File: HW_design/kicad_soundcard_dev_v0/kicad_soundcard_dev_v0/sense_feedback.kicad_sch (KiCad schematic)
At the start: 18 parts, among them U4 LSM6DSL, U5 ICP20100

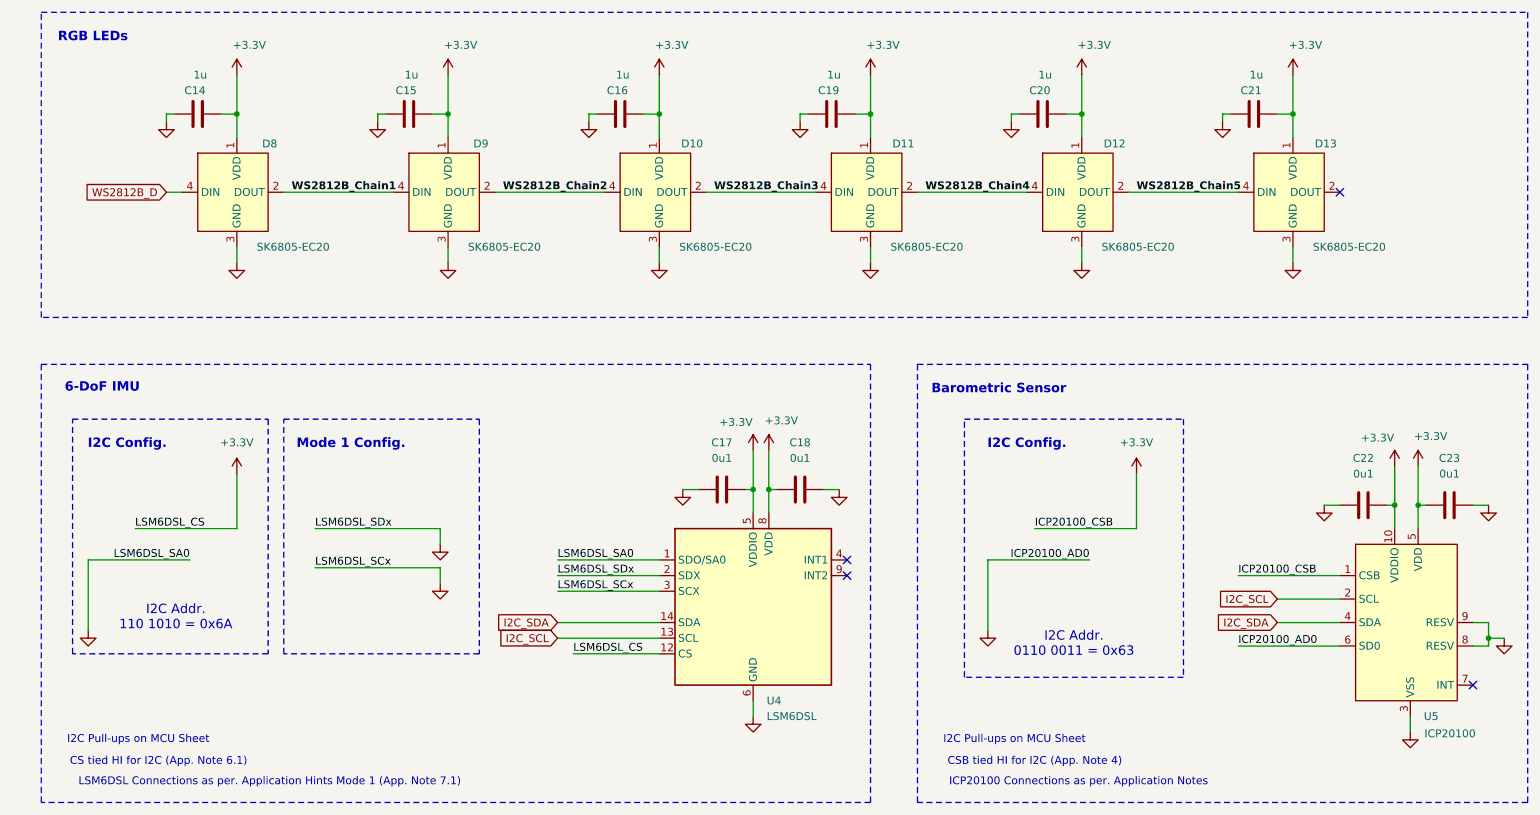
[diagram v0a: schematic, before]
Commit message: Schematic Rev2 + PCB Initial Release
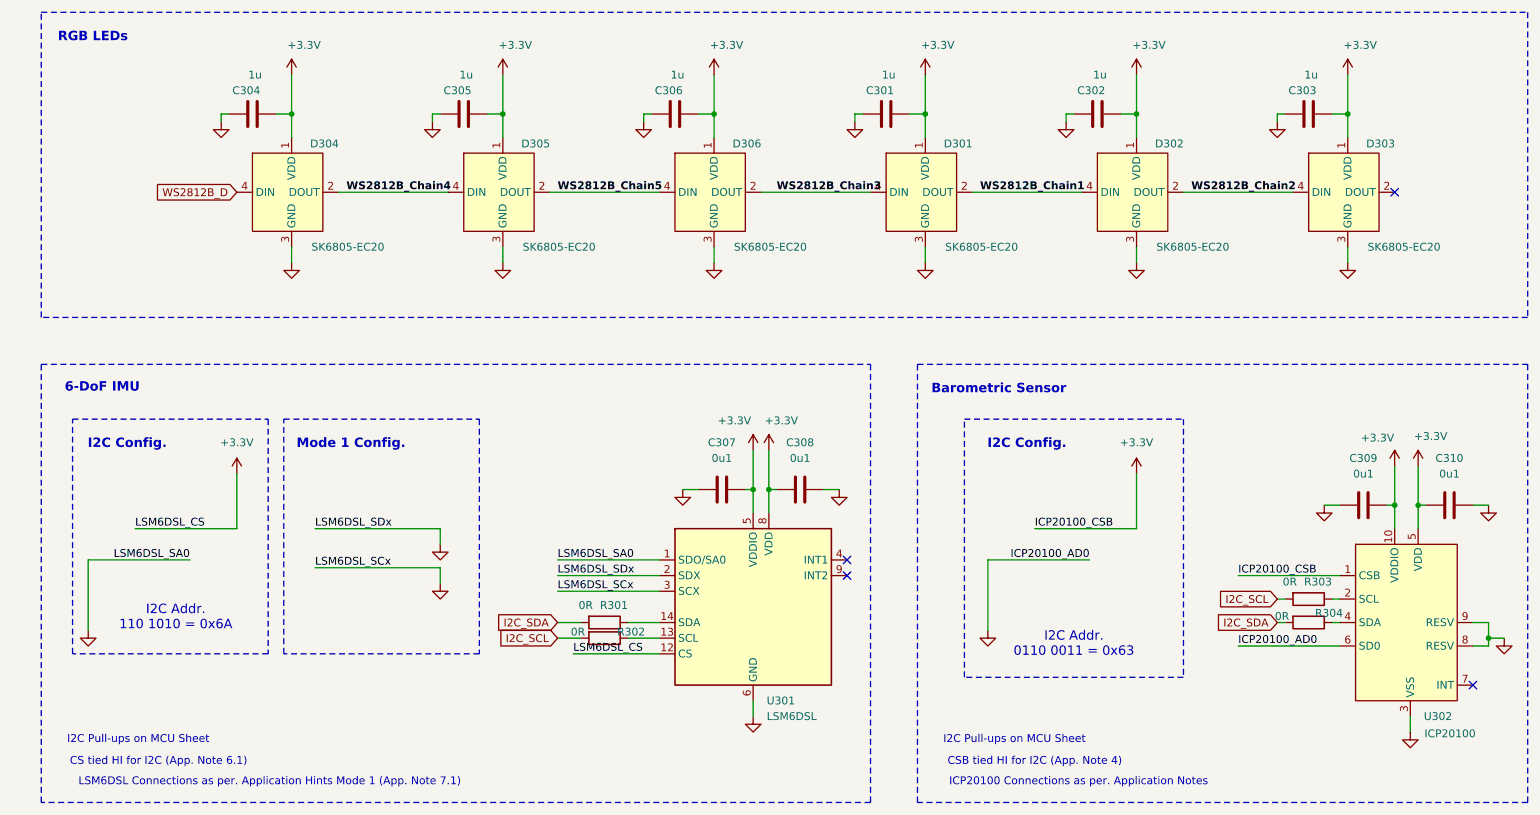
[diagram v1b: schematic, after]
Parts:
- added R301, R302, R303, R304: 0R, Resistor_SMD:R_0603_1608Metric, symbol Device:R
- renumbered C14 to C301, C15 to C302, C16 to C303, C19 to C304, C20 to C305, C21 to C306, C17 to C307, C18 to C308, C22 to C309, C23 to C310, D8 to D301, D9 to D302, D10 to D303, D11 to D304, D12 to D305, D13 to D306, U4 to U301, U5 to U302
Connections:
- net I2C_SCL: now also R302.2, R303.2; no longer U301.13 (SCL), U302.2 (SCL)
- net I2C_SDA: now also R301.2, R304.2; no longer U301.14 (SDA), U302.4 (SDA)
- net WS2812B_Chain3: now also D301.4 (DIN), D306.2 (DOUT); no longer D303.2 (DOUT), D304.4 (DIN)
- net WS2812B_D: now also D304.4 (DIN); no longer D301.4 (DIN)
- new net: R303.1, U302.2 (SCL)
- new net: R302.1, U301.13 (SCL)
- new net: R301.1, U301.14 (SDA)
- new net: R304.1, U302.4 (SDA)
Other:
- moved on the sheet: C301, C302, C303, C304, C305, C306, D301, D302, D303, D304, D305, D306

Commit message: Production JLCPCB V0
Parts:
- C301, C302, C303, C304, C305, C306: JLCPCB Link (none) -> https://jlcpcb.com/partdetail/15107-CL05A105KP5NNNC/C14445; Manufacturer (none) -> Samsung Electro-Mechanics; Manufacturer P/N (none) -> CL05A105KP5NNNC
- C307, C308, C309, C310: JLCPCB Link (none) -> https://jlcpcb.com/partdetail/1877-CL05B104KO5NNNC/C1525; Manufacturer (none) -> Samsung Electro-Mechanics; Manufacturer P/N (none) -> CL05B104KO5NNNC
- D301, D302, D303, D304, D305, D306: JLCPCB Link (none) -> https://jlcpcb.com/partdetail/OpscoOptoelectronics-SK6805EC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; Manufacturer (none) -> OPSCO Optoelectronics; Manufacturer P/N (none) -> SK6805-EC20
- R301, R302, R303, R304: JLCPCB Link (none) -> https://jlcpcb.com/partdetail/16080-0603WAJ0000T5E/C15402; Manufacturer (none) -> UNI-ROYAL(Uniroyal Elec); Manufacturer P/N (none) -> 0603WAJ0000T5E
- U301: JLCPCB Link (none) -> https://jlcpcb.com/partdetail/Stmicroelectronics-LSM6DSLTR/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; Manufacturer (none) -> STMicroelectronics; Manufacturer P/N (none) -> LSM6DSLTR
- U302: JLCPCB Link (none) -> https://jlcpcb.com/partdetail/TdkInvensense-ICP20100/C53435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; Manufacturer (none) -> TDK InvenSense; Manufacturer P/N (none) -> ICP-20100
